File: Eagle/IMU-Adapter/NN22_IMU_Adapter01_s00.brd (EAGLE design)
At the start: 63.5 x 33 mm, 90 parts, among them J1 M13X2_0.050_SHF, J2 M20X2_HARFLEX_M, J3 M04X2_0.050_SMD_NO_CREAM, J4 M04X2_0.050_SMD_NO_CREAM, J5 M03X1_JST_SH_RA, J6 USB-MICRO, U1 RP2040, U2 MCP1755_DFN, U3 W25Q_USON, U4 AP2265X_SOT, U5 ISM330DHCX, X1 CRYSTAL-3.2-2.5

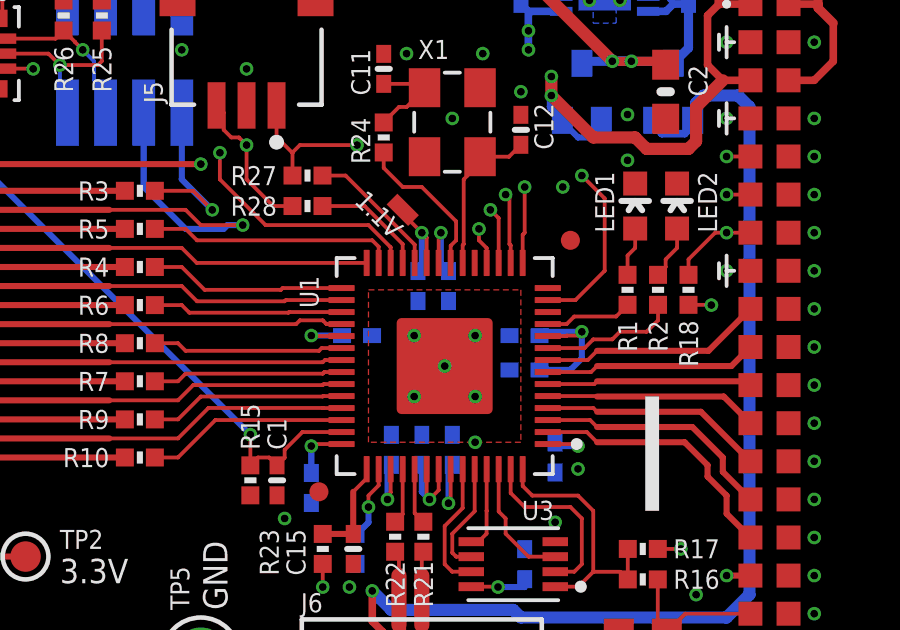
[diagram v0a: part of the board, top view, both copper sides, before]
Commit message: Small change in adapter copper pour.
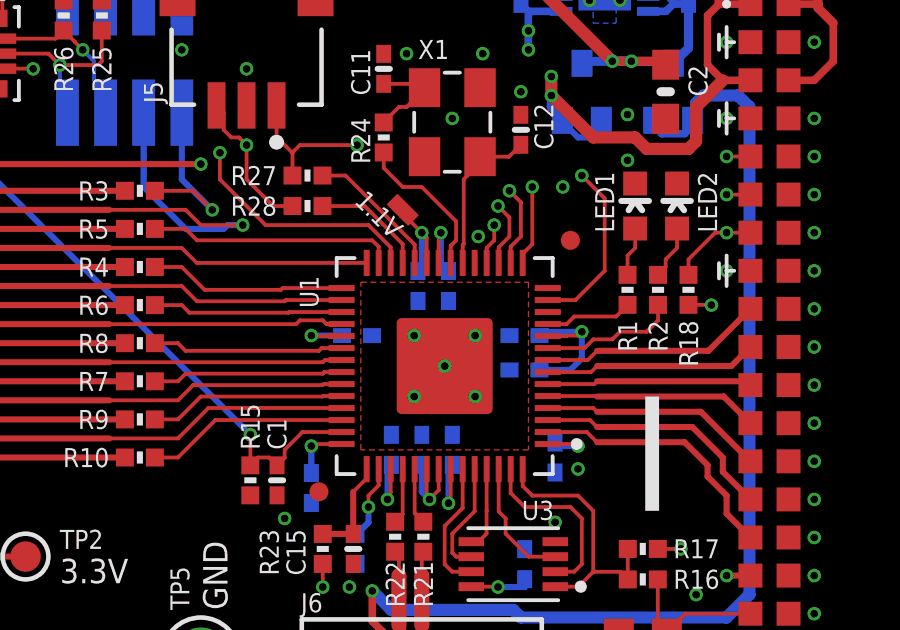
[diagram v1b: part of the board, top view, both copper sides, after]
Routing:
- net TX2: track 51.7 -> 52.2 mm
- net IMU_SCL: track 25.1 -> 25.6 mm
- net RX2_PRE: track 17.1 -> 17.6 mm
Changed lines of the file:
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@@
 <setting verticaltext="up"/>
 </settings>
-<grid distance="5" unitdist="mil" unit="mil" style="lines" multiple="2" display="yes" altdistance="5" altunitdist="mil" altunit="mil"/>
+<grid distance="5" unitdist="mil" unit="mil" style="lines" multiple="2" display="yes" altdistance="1" altunitdist="mil" altunit="mil"/>
 <layers>
 <layer number="1" name="Top" color="4" fill="1" visible="yes" active="yes"/>
@@
 <layer number="13" name="Route13" color="4" fill="5" visible="no" active="no"/>
 <layer number="14" name="Route14" color="1" fill="6" visible="no" active="no"/>
-<layer number="15" name="Route15" color="4" fill="6" visible="no" active="yes"/>
-<layer number="16" name="Bottom" color="1" fill="1" visible="yes" active="yes"/>
+<layer number="15" name="Route15" color="4" fill="6" visible="yes" active="yes"/>
+<layer number="16" name="Bottom" color="1" fill="1" visible="no" active="yes"/>
 <layer number="17" name="Pads" color="2" fill="1" visible="yes" active="yes"/>
 <layer number="18" name="Vias" color="2" fill="1" visible="yes" active="yes"/>
@@
 <via x="45.974" y="24.765" extent="1-16" drill="0.254"/>
 <via x="39.116" y="26.416" extent="1-16" drill="0.254"/>
-<via x="46.736" y="13.97" extent="1-16" drill="0.254"/>
 <via x="40.386" y="11.43" extent="1-16" drill="0.254"/>
 <via x="55.118" y="27.305" extent="1-16" drill="0.254"/>
@@
 <via x="62.738" y="22.86" extent="1-16" drill="0.254"/>
 <via x="62.738" y="29.21" extent="1-16" drill="0.254"/>
-<polygon width="0.127" layer="1" isolate="0.2032" thermals="no">
-<vertex x="43.18" y="19.05"/>
-<vertex x="48.26" y="19.05"/>
-<vertex x="48.26" y="13.97"/>
-<vertex x="43.18" y="13.97"/>
-</polygon>
 <via x="50.165" y="13.081" extent="1-16" drill="0.254"/>
 <via x="54.102" y="8.89" extent="1-16" drill="0.254"/>
@@
 <via x="35.687" y="30.226" extent="1-16" drill="0.254"/>
 <via x="36.957" y="27.051" extent="1-16" drill="0.254"/>
+<polygon width="0.127" layer="1" pour="cutout">
+<vertex x="42.926" y="19.304"/>
+<vertex x="48.514" y="19.304"/>
+<vertex x="48.514" y="13.716"/>
+<vertex x="42.926" y="13.716"/>
+</polygon>
+<via x="46.8376" y="20.828" extent="1-16" drill="0.254"/>
 </signal>
 <signal name="N$36">
@@
 <signal name="IMU_SCL">
 <contactref element="U1" pad="16"/>
-<via x="47.752" y="22.225" extent="1-16" drill="0.254"/>
-<wire x1="47.92" y1="19.9475" x2="47.92" y2="20.533" width="0.127" layer="1"/>
-<wire x1="47.92" y1="20.533" x2="47.879" y2="20.574" width="0.127" layer="1"/>
-<wire x1="47.879" y1="20.574" x2="47.879" y2="22.098" width="0.127" layer="1"/>
-<wire x1="47.879" y1="22.098" x2="47.752" y2="22.225" width="0.127" layer="1"/>
-<wire x1="47.752" y1="22.225" x2="37.211" y2="22.225" width="0.127" layer="15"/>
+<via x="47.879" y="22.352" extent="1-16" drill="0.254"/>
+<wire x1="47.879" y1="22.352" x2="46.99" y2="22.352" width="0.127" layer="15"/>
+<wire x1="46.99" y1="22.352" x2="46.863" y2="22.225" width="0.127" layer="15"/>
+<wire x1="46.863" y1="22.225" x2="37.211" y2="22.225" width="0.127" layer="15"/>
 <contactref element="U5" pad="13"/>
 <contactref element="R25" pad="1"/>
@@
 <wire x1="32.893" y1="26.543" x2="32.893" y2="25.2095" width="0.127" layer="16"/>
 <wire x1="32.893" y1="25.2095" x2="33.147" y2="24.9555" width="0.127" layer="16"/>
+<wire x1="48.26" y1="20.828" x2="48.26" y2="21.971" width="0.127" layer="1"/>
+<wire x1="48.26" y1="21.971" x2="47.879" y2="22.352" width="0.127" layer="1"/>
+<wire x1="47.92" y1="19.9475" x2="47.92" y2="20.488" width="0.127" layer="1"/>
+<wire x1="47.92" y1="20.488" x2="48.26" y2="20.828" width="0.127" layer="1"/>
 </signal>
 <signal name="RX4_PRE">
@@
 <contactref element="D3" pad="3"/>
 <contactref element="U1" pad="18"/>
-<via x="46.863" y="21.082" extent="1-16" drill="0.254"/>
-<wire x1="47.12" y1="19.9475" x2="47.12" y2="20.444" width="0.127" layer="1"/>
-<wire x1="47.12" y1="20.444" x2="46.863" y2="20.701" width="0.127" layer="1"/>
-<wire x1="46.863" y1="20.701" x2="46.863" y2="21.082" width="0.127" layer="1"/>
-<wire x1="46.863" y1="21.082" x2="46.482" y2="21.463" width="0.127" layer="15"/>
-<wire x1="46.482" y1="21.463" x2="39.243" y2="21.463" width="0.127" layer="15"/>
+<via x="47.371" y="21.209" extent="1-16" drill="0.254"/>
+<wire x1="47.371" y1="21.209" x2="47.117" y2="21.463" width="0.127" layer="15"/>
+<wire x1="47.117" y1="21.463" x2="39.243" y2="21.463" width="0.127" layer="15"/>
 <wire x1="39.243" y1="21.463" x2="38.989" y2="21.209" width="0.127" layer="15"/>
 <via x="38.989" y="21.209" extent="1-16" drill="0.254"/>
@@
 <wire x1="38.354" y1="21.082" x2="38.481" y2="21.209" width="0.2032" layer="16"/>
 <wire x1="38.481" y1="21.209" x2="38.989" y2="21.209" width="0.2032" layer="16"/>
+<wire x1="47.12" y1="19.9475" x2="47.12" y2="20.45" width="0.127" layer="1"/>
+<wire x1="47.12" y1="20.45" x2="47.371" y2="20.701" width="0.127" layer="1"/>
+<wire x1="47.371" y1="20.701" x2="47.371" y2="21.209" width="0.127" layer="1"/>
 </signal>
 <signal name="TX1">
@@
 <contactref element="R3" pad="2"/>
 <contactref element="U1" pad="17"/>
-<via x="47.244" y="21.717" extent="1-16" drill="0.254"/>
-<wire x1="47.52" y1="19.9475" x2="47.52" y2="21.441" width="0.127" layer="1"/>
-<wire x1="47.52" y1="21.441" x2="47.244" y2="21.717" width="0.127" layer="1"/>
-<wire x1="47.244" y1="21.717" x2="46.863" y2="21.717" width="0.127" layer="15"/>
-<wire x1="46.863" y1="21.717" x2="46.736" y2="21.844" width="0.127" layer="15"/>
-<wire x1="46.736" y1="21.844" x2="38.1" y2="21.844" width="0.127" layer="15"/>
+<via x="47.498" y="21.844" extent="1-16" drill="0.254"/>
+<wire x1="47.498" y1="21.844" x2="38.1" y2="21.844" width="0.127" layer="15"/>
 <wire x1="38.1" y1="21.844" x2="37.973" y2="21.717" width="0.127" layer="15"/>
 <via x="37.973" y="21.717" extent="1-16" drill="0.254"/>
@@
 <wire x1="36.957" y1="24.9555" x2="36.957" y2="22.733" width="0.2032" layer="16"/>
 <wire x1="36.957" y1="22.733" x2="37.973" y2="21.717" width="0.2032" layer="16"/>
+<wire x1="47.52" y1="19.9475" x2="47.52" y2="20.469" width="0.127" layer="1"/>
+<wire x1="47.52" y1="20.469" x2="47.879" y2="20.828" width="0.127" layer="1"/>
+<wire x1="47.879" y1="20.828" x2="47.879" y2="21.463" width="0.127" layer="1"/>
+<wire x1="47.879" y1="21.463" x2="47.498" y2="21.844" width="0.127" layer="1"/>
 </signal>
 <signal name="N$6">
@@
 <contactref element="R26" pad="1"/>
 <contactref element="U1" pad="15"/>
-<wire x1="48.32" y1="19.9475" x2="48.32" y2="20.888" width="0.127" layer="1"/>
-<via x="48.387" y="22.479" extent="1-16" drill="0.254"/>
-<wire x1="47.371" y1="22.733" x2="47.244" y2="22.606" width="0.127" layer="15"/>
-<wire x1="47.244" y1="22.606" x2="37.465" y2="22.606" width="0.127" layer="15"/>
-<wire x1="48.32" y1="20.888" x2="48.387" y2="20.955" width="0.127" layer="1"/>
-<wire x1="48.387" y1="20.955" x2="48.387" y2="22.479" width="0.127" layer="1"/>
-<wire x1="47.371" y1="22.733" x2="48.133" y2="22.733" width="0.127" layer="15"/>
-<wire x1="48.133" y1="22.733" x2="48.387" y2="22.479" width="0.127" layer="15"/>
+<via x="48.641" y="22.479" extent="1-16" drill="0.254"/>
+<wire x1="46.9138" y1="22.7838" x2="46.736" y2="22.606" width="0.127" layer="15"/>
+<wire x1="46.736" y1="22.606" x2="37.465" y2="22.606" width="0.127" layer="15"/>
+<wire x1="48.641" y1="20.574" x2="48.641" y2="22.479" width="0.127" layer="1"/>
+<wire x1="46.9138" y1="22.7838" x2="48.3362" y2="22.7838" width="0.127" layer="15"/>
+<wire x1="48.3362" y1="22.7838" x2="48.641" y2="22.479" width="0.127" layer="15"/>
 <wire x1="37.465" y1="22.606" x2="33.655" y2="26.416" width="0.127" layer="15"/>
 <wire x1="33.655" y1="26.416" x2="33.655" y2="27.051" width="0.127" layer="15"/>
@@
 <wire x1="34.036" y1="26.035" x2="34.036" y2="26.67" width="0.127" layer="16"/>
 <wire x1="34.036" y1="26.67" x2="33.655" y2="27.051" width="0.127" layer="16"/>
+<wire x1="48.32" y1="19.9475" x2="48.32" y2="20.253" width="0.127" layer="1"/>
+<wire x1="48.32" y1="20.253" x2="48.641" y2="20.574" width="0.127" layer="1"/>
 </signal>
 <signal name="SWDIO_PRE">
